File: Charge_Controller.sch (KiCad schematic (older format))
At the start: 137 parts, among them J1 SOLAR, J10 Conn_01x01_Female, J11 Conn_01x01_Female, J12 Conn_01x01_Female, J13 Conn_01x01_Female, J14 Conn_01x01_Female, J15 Conn_01x01_Female, J16 Conn_01x01_Female, J17 Conn_01x01_Female, J18 Conn_01x01_Female, J19 Conn_01x01_Female, J2 Conn_01x01_Female, J20 Conn_01x01_Female, J21 Conn_01x01_Female, J22 Conn_01x01_Female, J23 Conn_01x01_Female, J24 Conn_01x01_Female, J25 Conn_01x01_Female, J26 Conn_01x01_Female, J27 Conn_01x01_Female, J28 Conn_01x01_Female, J29 Conn_01x01_Female, J3 Conn_01x01_Female, J30 Conn_01x01_Female, J31 Conn_01x01_Female, J32 Conn_01x01_Female, J33 SOLAR, J34 BATT, J4 Conn_01x01_Female, J5 Conn_01x01_Female, J6 Conn_01x01_Female, J7 Conn_01x01_Female, J8 BATT, J9 USB_OTG, Q1 CSD19505, Q2 CSD19505, Q3 CSD19505, Q4 Si2306, Q5 2N3904, Q6 2N3904, Q7 PMOS-100V-90A, Q8 PMOS-100V-90A, U1 ACS712-30A, U10 ADS1015, U11 NUP4202, U2 B1212, U3 AMS1117-5.0, U4 AMS1117-3.3, U5 XL7005A, U6 XL7005A, U7 IR2104, U8 ESP32-WROOM-32, U9 CH340G

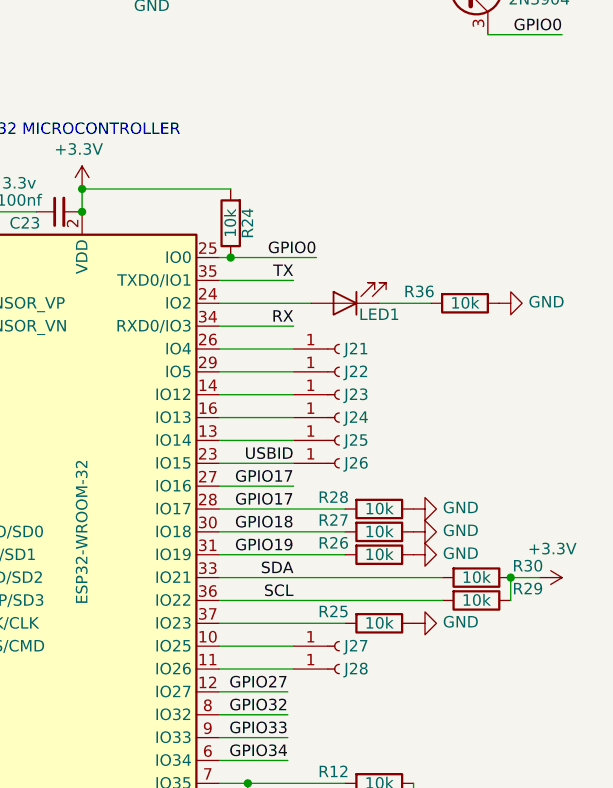
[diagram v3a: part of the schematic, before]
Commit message: Added FAN controller circuit
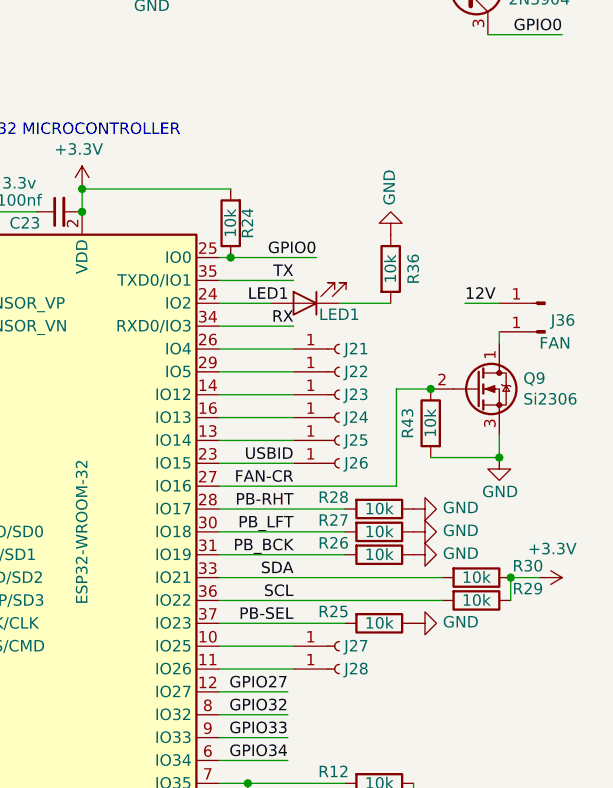
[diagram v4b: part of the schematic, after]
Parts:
- added J35: BATT, TestPoint:TestPoint_Keystone_5005-5009_Compact, symbol Connector:Conn_01x01_Male
- added J36: FAN, TestPoint:TestPoint_Keystone_5005-5009_Compact, symbol Connector:Conn_01x01_Male
- added Q9: Si2306, Package_TO_SOT_SMD:SOT-23, symbol Device:Q_NMOS_DGS
- added R43: 10k, Resistor_SMD:R_0805_2012Metric, symbol Device:R
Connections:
- net 12V: now also J35.1 (Pin_1)
- net GND: now also Q9.3 (S), R43.2
- net LED1: now reaches LED1.2 (A), U8.24 (IO2)
- net PB-SEL: now reaches R25.2, U8.37 (IO23)
- net GPIO17 renamed PB-RHT
- net PB-RHT: no longer U8.27 (IO16)
- net GPIO18 renamed PB_LFT
- net GPIO19 renamed PB_BCK
- new net: J36.1 (Pin_1), Q9.1 (D)
- new net FAN-CR: Q9.2 (G), R43.1, U8.27 (IO16)
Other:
- moved on the sheet: LED1, R36
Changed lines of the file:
@@
 L Device:LED LED1
 U 1 1 62F625A5
-P 9425 4050
-F 0 "LED1" H 9275 4100 50  0000 C CNN
-F 1 "LED" H 9418 3886 50  0001 C CNN
-F 2 "LED_SMD:LED_0805_2012Metric" H 9425 4050 50  0001 C CNN
-F 3 "~" H 9425 4050 50  0001 C CNN
-F 4 "C84256" H 9425 4050 50  0001 C CNN "jlcpcb"
-	1    9425 4050
+P 9250 4050
+F 0 "LED1" H 9100 4100 50  0000 C CNN
+F 1 "LED" H 9243 3886 50  0001 C CNN
+F 2 "LED_SMD:LED_0805_2012Metric" H 9250 4050 50  0001 C CNN
+F 3 "~" H 9250 4050 50  0001 C CNN
+F 4 "C84256" H 9250 4050 50  0001 C CNN "jlcpcb"
+	1    9250 4050
 	-1   0    0    1
 $EndComp
@@
 L Device:R R36
 U 1 1 62F6379F
-P 9950 4050
-F 0 "R36" V 9900 3850 50  0000 C CNN
-F 1 "10k" V 9950 4050 50  0000 C CNN
-F 2 "Resistor_SMD:R_0805_2012Metric" V 9880 4050 50  0001 C CNN
-F 3 "~" H 9950 4050 50  0001 C CNN
-F 4 "C17724" H 9950 4050 50  0001 C CNN "jlcpcb"
-	1    9950 4050
-	0    1    1    0
+P 9625 3900
+F 0 "R36" V 9725 3900 50  0000 C CNN
+F 1 "10k" V 9625 3900 50  0000 C CNN
+F 2 "Resistor_SMD:R_0805_2012Metric" V 9555 3900 50  0001 C CNN
+F 3 "~" H 9625 3900 50  0001 C CNN
+F 4 "C17724" H 9625 3900 50  0001 C CNN "jlcpcb"
+	1    9625 3900
+	1    0    0    -1
 $EndComp
 $Comp
 L power:GND #PWR033
 U 1 1 62F64399
-P 10100 4050
-F 0 "#PWR033" H 10100 3800 50  0001 C CNN
-F 1 "GND" V 10105 3922 50  0000 R CNN
-F 2 "" H 10100 4050 50  0001 C CNN
-F 3 "" H 10100 4050 50  0001 C CNN
-	1    10100 4050
-	0    -1   -1   0
+P 9625 3750
+F 0 "#PWR033" H 9625 3500 50  0001 C CNN
+F 1 "GND" V 9630 3622 50  0000 R CNN
+F 2 "" H 9625 3750 50  0001 C CNN
+F 3 "" H 9625 3750 50  0001 C CNN
+	1    9625 3750
+	-1   0    0    1
 $EndComp
 $Comp
@@
 $EndComp
 Wire Wire Line
-	9575 4050 9800 4050
+	9400 4050 9625 4050
 $Comp
 L power:GND #PWR024
@@
 Connection ~ 8275 3550
 Wire Wire Line
-	8875 4050 9275 4050
+	8875 4050 9100 4050
 Wire Wire Line
 	9200 3950 8875 3950
@@
 A3
 Text Label 9200 5050 2    50   ~ 0
-GPIO18
+PB_LFT
 Wire Wire Line
 	8875 6050 9175 6050
-Text Label 9200 4950 2    50   ~ 0
-GPIO17
 Text Label 9200 5150 2    50   ~ 0
-GPIO19
+PB_BCK
 Text Label 9200 4850 2    50   ~ 0
-GPIO17
-Wire Wire Line
-	8875 4850 9200 4850
+FAN-CR
 Text Label 9175 5750 2    50   ~ 0
 GPIO27
@@
 	-1   0    0    -1
 $EndComp
+Text Label 9200 5450 2    50   ~ 0
+PB-SEL
+Text Label 9200 4950 2    50   ~ 0
+PB-RHT
+$Comp
+L Device:Q_NMOS_DGS Q9
+U 1 1 63E86110
+P 10000 4425
+F 0 "Q9" H 10205 4471 50  0000 L CNN
+F 1 "Si2306" H 10205 4380 50  0000 L CNN
+F 2 "Package_TO_SOT_SMD:SOT-23" H 10200 4525 50  0001 C CNN
+F 3 "~" H 10000 4425 50  0001 C CNN
+F 4 "C347489" H 10000 4425 50  0001 C CNN "jlcpcb"
+	1    10000 4425
+	1    0    0    -1
+$EndComp
+$Comp
+L Device:R R43
+U 1 1 63E8611B
+P 9800 4575
+F 0 "R43" V 9900 4575 50  0000 C CNN
+F 1 "10k" V 9800 4575 50  0000 C CNN
+F 2 "Resistor_SMD:R_0805_2012Metric" V 9730 4575 50  0001 C CNN
+F 3 "~" H 9800 4575 50  0001 C CNN
+F 4 "C17724" H 9800 4575 50  0001 C CNN "jlcpcb"
+	1    9800 4575
+	-1   0    0    -1
+$EndComp
+$Comp
+L power:GND #PWR036
+U 1 1 63E86125
+P 10100 4725
+F 0 "#PWR036" H 10100 4475 50  0001 C CNN
+F 1 "GND" H 10175 4575 50  0000 R CNN
+F 2 "" H 10100 4725 50  0001 C CNN
+F 3 "" H 10100 4725 50  0001 C CNN
+	1    10100 4725
+	-1   0    0    -1
+$EndComp
+Wire Wire Line
+	10100 4625 10100 4725
+Wire Wire Line
+	10100 4725 9800 4725
+Connection ~ 10100 4725
+$Comp
+L Connector:Conn_01x01_Male J36
+U 1 1 63EDFCB9
+P 10300 4175
+F 0 "J36" H 10275 4225 50  0000 R CNN
+F 1 "FAN" H 10325 4125 50  0000 R CNN
+F 2 "TestPoint:TestPoint_Keystone_5005-5009_Compact" H 10300 4175 50  0001 C CNN
+F 3 "~" H 10300 4175 50  0001 C CNN
+F 4 "277-13746-ND" H 10300 4175 50  0001 C CNN "Digikey"
+F 5 "NA" H 10300 4175 50  0001 C CNN "jlcpcb"
+	1    10300 4175
+	-1   0    0    -1
+$EndComp
+Wire Wire Line
+	10100 4225 10100 4175
+$Comp
+L Connector:Conn_01x01_Male J35
+U 1 1 63EF7567
+P 10300 4050
+F 0 "J35" H 10275 4000 50  0001 R CNN
+F 1 "BATT" H 10325 4000 50  0001 R CNN
+F 2 "TestPoint:TestPoint_Keystone_5005-5009_Compact" H 10300 4050 50  0001 C CNN
+F 3 "~" H 10300 4050 50  0001 C CNN
+F 4 "NA" H 10300 4050 50  0001 C CNN "Digikey"
+F 5 "NA" H 10300 4050 50  0001 C CNN "jlcpcb"
+	1    10300 4050
+	-1   0    0    -1
+$EndComp
+Text Label 9000 4050 0    50   ~ 0
+LED1
+Text Label 9950 4050 0    50   ~ 0
+12V
+Wire Wire Line
+	9950 4050 10100 4050
+Wire Wire Line
+	9650 4850 9650 4425
+Wire Wire Line
+	9650 4425 9800 4425
+Wire Wire Line
+	8875 4850 9650 4850
+Connection ~ 9800 4425
 $EndSCHEMATC

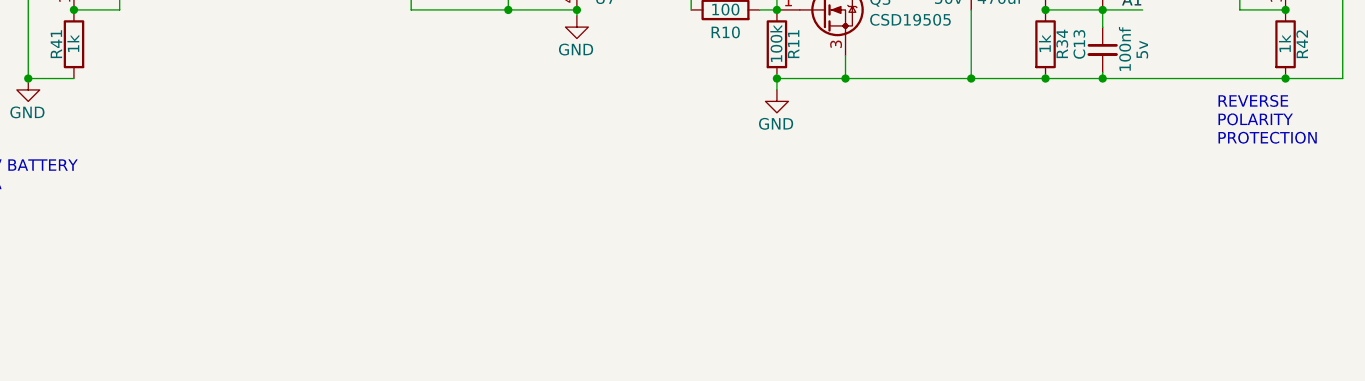
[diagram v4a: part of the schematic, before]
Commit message: Added push buttons, LCD connector, and fan MOSFET to schematic.
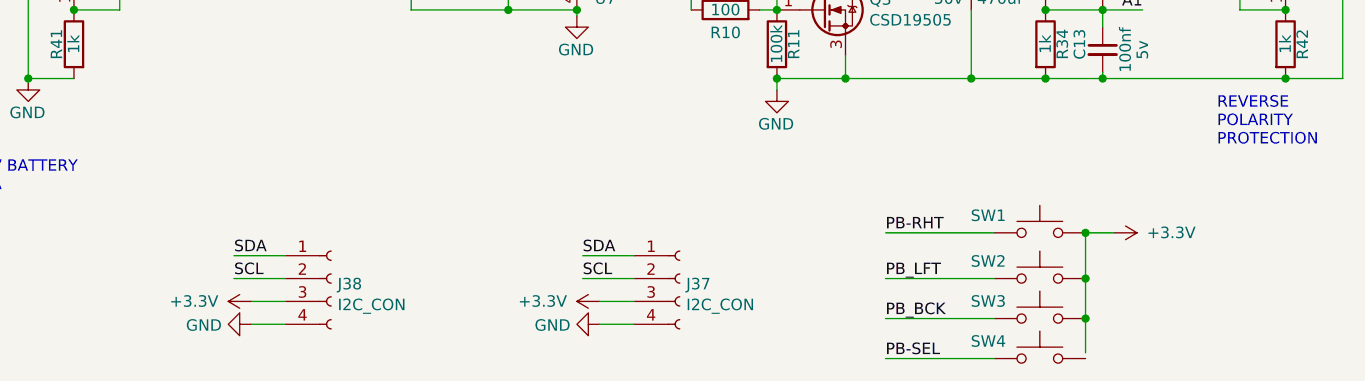
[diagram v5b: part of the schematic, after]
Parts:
- added J37, J38: I2C_CON, Connector_PinHeader_2.54mm:PinHeader_1x04_P2.54mm_Vertical, symbol Connector:Conn_01x04_Female
- added SW1, SW2, SW3, SW4: RIGHT, Button_Switch_SMD:SW_SPST_EVQQ2, symbol Switch:SW_Push
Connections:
- net +3V3: now also J37.3 (Pin_3), J38.3 (Pin_3), SW1.2, SW2.2, SW3.2
- net GND: now also J37.4 (Pin_4), J38.4 (Pin_4)
- net PB-RHT: now also SW1.1
- net PB-SEL: now also SW4.1
- net PB_BCK: now also SW3.1
- net PB_LFT: now also SW2.1
- net SCL: now also J37.2 (Pin_2), J38.2 (Pin_2)
- net SDA: now also J37.1 (Pin_1), J38.1 (Pin_1)
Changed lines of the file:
@@
 	8875 4850 9650 4850
 Connection ~ 9800 4425
+$Comp
+L Switch:SW_Push SW1
+U 1 1 63F5793F
+P 5325 7275
+F 0 "SW1" H 5100 7350 50  0000 C CNN
+F 1 "RIGHT" H 5325 7469 50  0001 C CNN
+F 2 "Button_Switch_SMD:SW_SPST_EVQQ2" H 5325 7475 50  0001 C CNN
+F 3 "~" H 5325 7475 50  0001 C CNN
+F 4 "C318884" H 5325 7275 50  0001 C CNN "jlcpcb"
+	1    5325 7275
+	1    0    0    -1
+$EndComp
+$Comp
+L Switch:SW_Push SW2
+U 1 1 63F5DE3C
+P 5325 7475
+F 0 "SW2" H 5100 7550 50  0000 C CNN
+F 1 "RIGHT" H 5325 7669 50  0001 C CNN
+F 2 "Button_Switch_SMD:SW_SPST_EVQQ2" H 5325 7675 50  0001 C CNN
+F 3 "~" H 5325 7675 50  0001 C CNN
+F 4 "C318884" H 5325 7475 50  0001 C CNN "jlcpcb"
+	1    5325 7475
+	1    0    0    -1
+$EndComp
+$Comp
+L Switch:SW_Push SW3
+U 1 1 63F5EAD2
+P 5325 7650
+F 0 "SW3" H 5100 7725 50  0000 C CNN
+F 1 "RIGHT" H 5325 7844 50  0001 C CNN
+F 2 "Button_Switch_SMD:SW_SPST_EVQQ2" H 5325 7850 50  0001 C CNN
+F 3 "~" H 5325 7850 50  0001 C CNN
+F 4 "C318884" H 5325 7650 50  0001 C CNN "jlcpcb"
+	1    5325 7650
+	1    0    0    -1
+$EndComp
+$Comp
+L Switch:SW_Push SW4
+U 1 1 63F5EDED
+P 5325 7825
+F 0 "SW4" H 5100 7900 50  0000 C CNN
+F 1 "RIGHT" H 5325 8019 50  0001 C CNN
+F 2 "Button_Switch_SMD:SW_SPST_EVQQ2" H 5325 8025 50  0001 C CNN
+F 3 "~" H 5325 8025 50  0001 C CNN
+F 4 "C318884" H 5325 7825 50  0001 C CNN "jlcpcb"
+	1    5325 7825
+	1    0    0    -1
+$EndComp
+$Comp
+L Connector:Conn_01x04_Female J37
+U 1 1 63F60120
+P 3750 7475
+F 0 "J37" H 3778 7451 50  0000 L CNN
+F 1 "I2C_CON" H 3778 7360 50  0000 L CNN
+F 2 "Connector_PinHeader_2.54mm:PinHeader_1x04_P2.54mm_Vertical" H 3750 7475 50  0001 C CNN
+F 3 "~" H 3750 7475 50  0001 C CNN
+	1    3750 7475
+	1    0    0    -1
+$EndComp
+Text Label 3325 7375 0    50   ~ 0
+SDA
+Text Label 3325 7475 0    50   ~ 0
+SCL
+$Comp
+L power:+3.3V #PWR037
+U 1 1 63F60F19
+P 3400 7575
+F 0 "#PWR037" H 3400 7425 50  0001 C CNN
+F 1 "+3.3V" V 3400 7825 50  0000 C CNN
+F 2 "" H 3400 7575 50  0001 C CNN
+F 3 "" H 3400 7575 50  0001 C CNN
+	1    3400 7575
+	0    -1   1    0
+$EndComp
+$Comp
+L power:GND #PWR038
+U 1 1 63F6180B
+P 3400 7675
+F 0 "#PWR038" H 3400 7425 50  0001 C CNN
+F 1 "GND" V 3405 7547 50  0000 R CNN
+F 2 "" H 3400 7675 50  0001 C CNN
+F 3 "" H 3400 7675 50  0001 C CNN
+	1    3400 7675
+	0    1    1    0
+$EndComp
+Wire Wire Line
+	3325 7375 3550 7375
+Wire Wire Line
+	3325 7475 3550 7475
+Wire Wire Line
+	3400 7575 3550 7575
+Wire Wire Line
+	3400 7675 3550 7675
+$Comp
+L power:+3.3V #PWR039
+U 1 1 63FDD2A6
+P 5650 7275
+F 0 "#PWR039" H 5650 7125 50  0001 C CNN
+F 1 "+3.3V" V 5650 7525 50  0000 C CNN
+F 2 "" H 5650 7275 50  0001 C CNN
+F 3 "" H 5650 7275 50  0001 C CNN
+	1    5650 7275
+	0    1    -1   0
+$EndComp
+Wire Wire Line
+	5525 7800 5525 7650
+Wire Wire Line
+	5525 7275 5650 7275
+Connection ~ 5525 7275
+Connection ~ 5525 7475
+Wire Wire Line
+	5525 7475 5525 7275
+Connection ~ 5525 7650
+Wire Wire Line
+	5525 7650 5525 7475
+Text Label 4650 7275 0    50   ~ 0
+PB-RHT
+Text Label 4650 7475 0    50   ~ 0
+PB_LFT
+Text Label 4650 7650 0    50   ~ 0
+PB_BCK
+Text Label 4650 7825 0    50   ~ 0
+PB-SEL
+Wire Wire Line
+	4650 7825 5125 7825
+Wire Wire Line
+	4650 7650 5125 7650
+Wire Wire Line
+	4650 7475 5125 7475
+Wire Wire Line
+	4650 7275 5125 7275
+$Comp
+L Connector:Conn_01x04_Female J38
+U 1 1 64093FFC
+P 2225 7475
+F 0 "J38" H 2253 7451 50  0000 L CNN
+F 1 "I2C_CON" H 2253 7360 50  0000 L CNN
+F 2 "Connector_PinHeader_2.54mm:PinHeader_1x04_P2.54mm_Vertical" H 2225 7475 50  0001 C CNN
+F 3 "~" H 2225 7475 50  0001 C CNN
+	1    2225 7475
+	1    0    0    -1
+$EndComp
+Text Label 1800 7375 0    50   ~ 0
+SDA
+Text Label 1800 7475 0    50   ~ 0
+SCL
+$Comp
+L power:+3.3V #PWR040
+U 1 1 64094008
+P 1875 7575
+F 0 "#PWR040" H 1875 7425 50  0001 C CNN
+F 1 "+3.3V" V 1875 7825 50  0000 C CNN
+F 2 "" H 1875 7575 50  0001 C CNN
+F 3 "" H 1875 7575 50  0001 C CNN
+	1    1875 7575
+	0    -1   1    0
+$EndComp
+$Comp
+L power:GND #PWR041
+U 1 1 64094012
+P 1875 7675
+F 0 "#PWR041" H 1875 7425 50  0001 C CNN
+F 1 "GND" V 1880 7547 50  0000 R CNN
+F 2 "" H 1875 7675 50  0001 C CNN
+F 3 "" H 1875 7675 50  0001 C CNN
+	1    1875 7675
+	0    1    1    0
+$EndComp
+Wire Wire Line
+	1800 7375 2025 7375
+Wire Wire Line
+	1800 7475 2025 7475
+Wire Wire Line
+	1875 7575 2025 7575
+Wire Wire Line
+	1875 7675 2025 7675
 $EndSCHEMATC

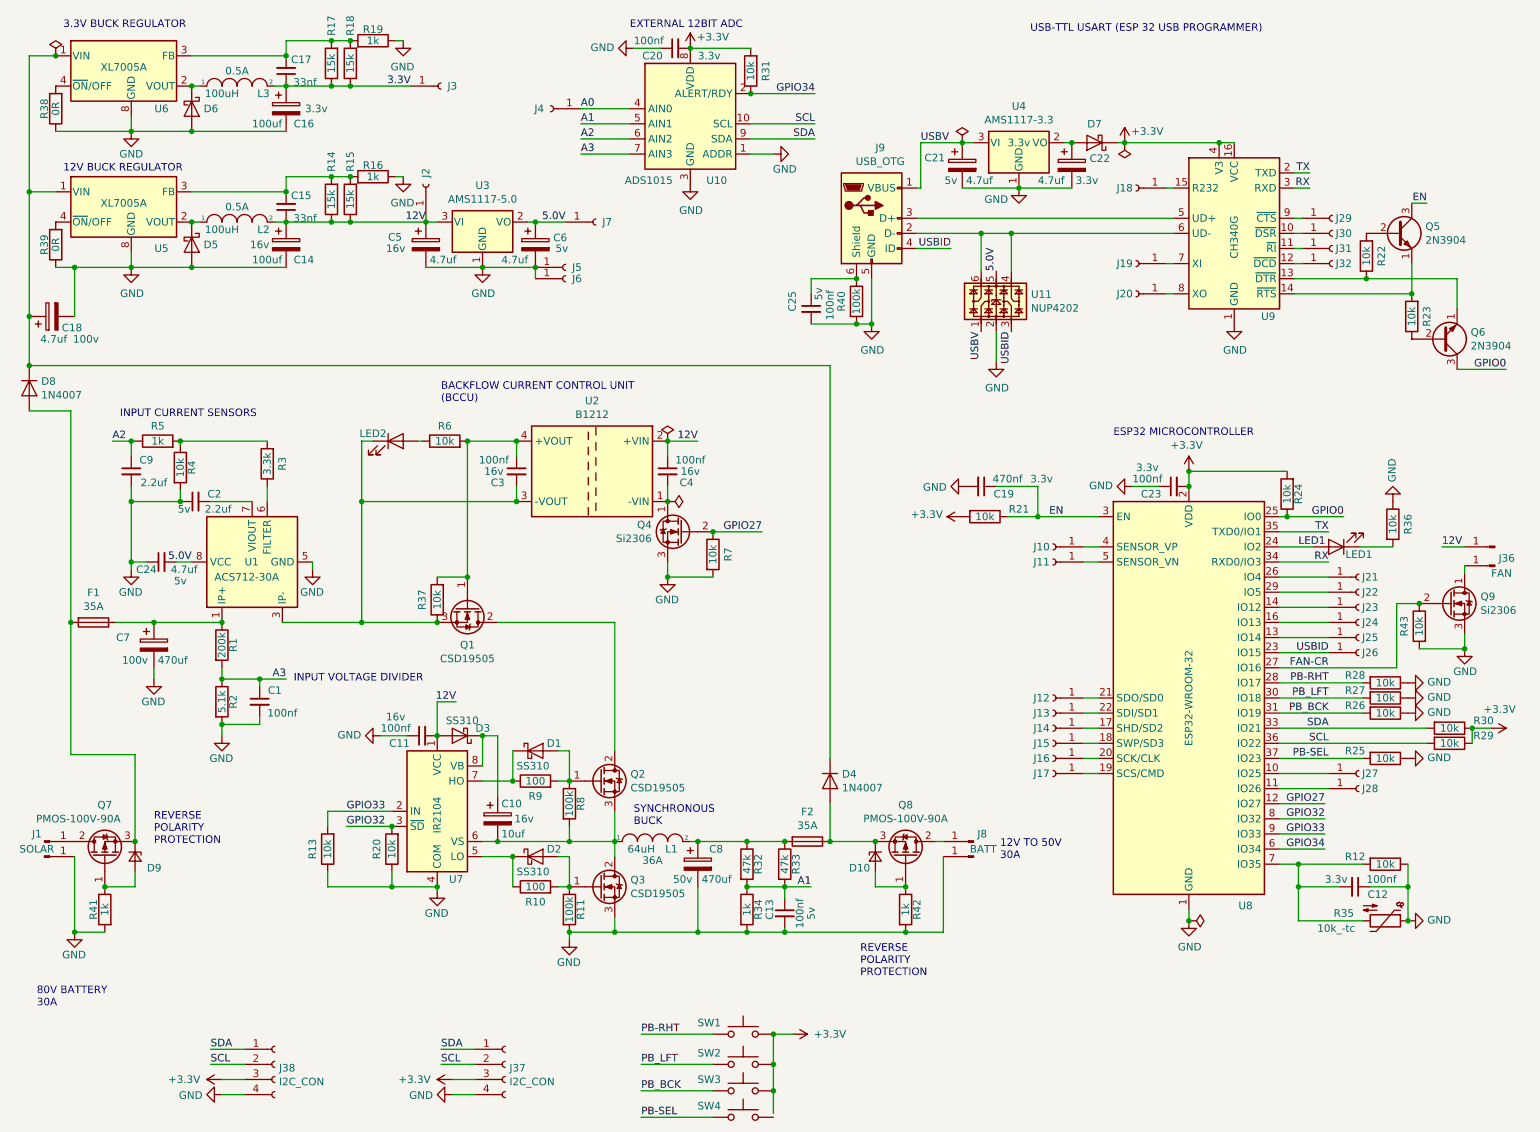
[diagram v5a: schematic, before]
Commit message: Started layout of PCB, first grouping of components.
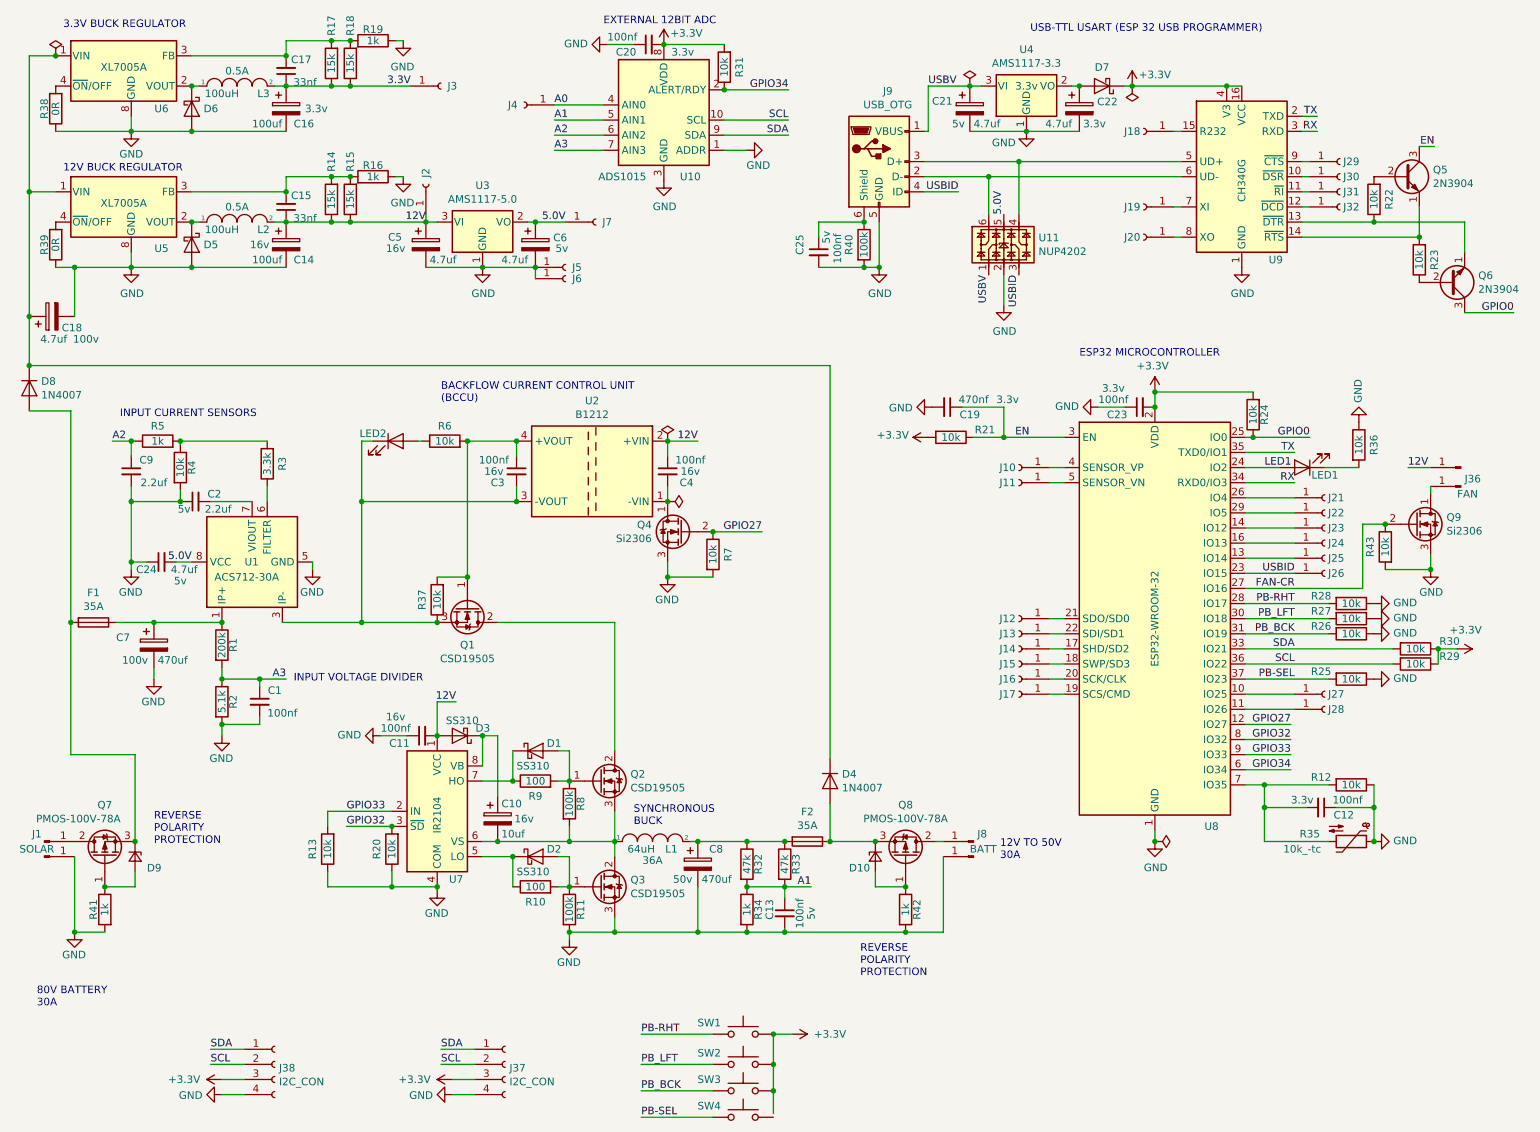
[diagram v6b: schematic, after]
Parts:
- D10, D9: footprint Diode_SMD:D_MELF-RM10_Universal_Handsoldering -> Diode_SMD:D_MiniMELF_Handsoldering
- Q7, Q8: value PMOS-100V-90A -> PMOS-100V-78A; footprint Package_TO_SOT_SMD:TO-263-2 -> Package_TO_SOT_SMD:TO-252-2; jlcpcb C468007 -> C216784
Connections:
- net at J9.3 (D+), U9.5 (UD+): now also U11.4
- net at J9.2 (D-), U11.6, U9.6 (UD-): no longer U11.4
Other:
- moved on the sheet: C12, C19, C20, C21, C22, C23, C25, D7, J10, J11, J12, J13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
